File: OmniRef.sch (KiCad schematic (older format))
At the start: 38 parts, among them J1 4mm Banana Jack Pair, J2 4mm Banana Jack Pair, Q1 PMBT3906, SW1 SW_SPDT, U1 REFERENCE IC, U2 LP2951, U3 REFERENCE IC

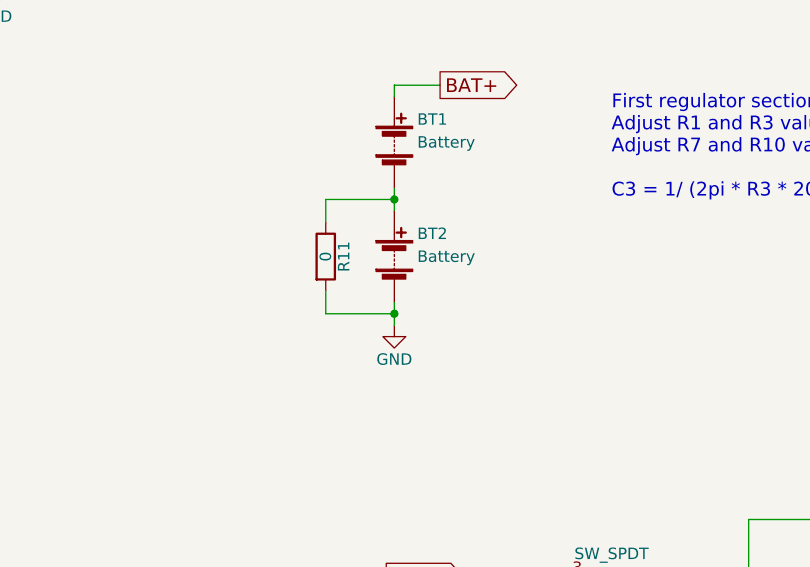
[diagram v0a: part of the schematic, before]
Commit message: Renamed to OmniRef.  Made some final changes to schematic and board before generating gerbers.
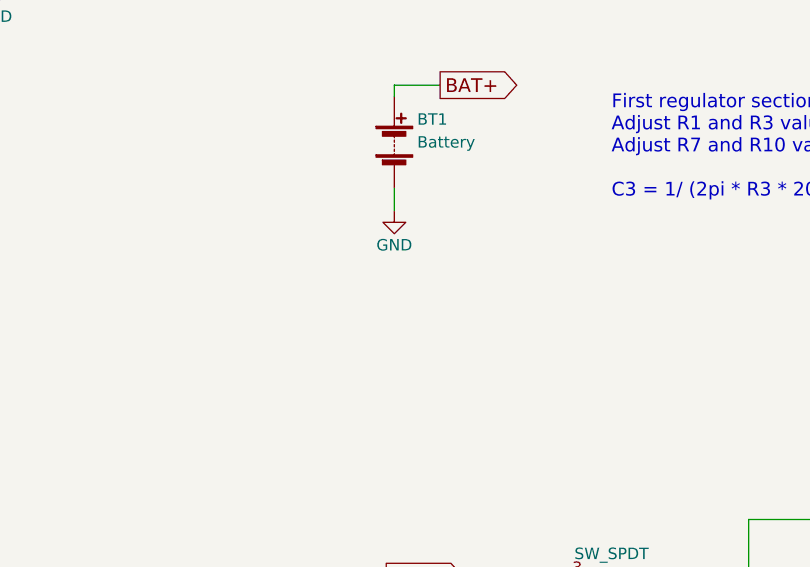
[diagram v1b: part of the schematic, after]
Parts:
- removed BT2: Battery, _NTSFootprints:9vClipWireLeads, symbol Battery
- removed R11: 0, Resistors_SMD:R_0805_HandSoldering, symbol R
- D5, D7: footprint _NTSFootprints:LED_1206_1.7mmHole -> _NTSFootprints:LED_1206_2.15mmHole
- J1: footprint _NTSFootprints:Banana_Jack_2pin_.25_.75 -> _NTSFootprints:Banana_Jack_2pin_Wings_45M_.25_.75
- J2: footprint _NTSFootprints:Banana_Jack_2pin_.25_.75 -> _NTSFootprints:Banana_Jack_2pin_Wings_.25_.75
- SW1: footprint Buttons_Switches_THT:SW_CuK_JS202011CQN_DPDT_Straight -> _NTSFootprints:CnK_L_Series_DPDT
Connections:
- net GND: now also BT1.2 (-)
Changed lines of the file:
@@
 LIBS:elec-unifil
 LIBS:switches
-LIBS:VoltageReference-cache
+LIBS:OmniRef-cache
 EELAYER 25 0
 EELAYER END
@@
 F 0 "D5" H 6550 4350 50  0000 C CNN
 F 1 "LED" H 6550 4150 50  0000 C CNN
-F 2 "_NTSFootprints:LED_1206_1.7mmHole" H 6550 4250 50  0001 C CNN
+F 2 "_NTSFootprints:LED_1206_2.15mmHole" H 6550 4250 50  0001 C CNN
 F 3 "" H 6550 4250 50  0000 C CNN
 	1    6550 4250
@@
 F 0 "J1" H 1150 4300 50  0000 C TNN
 F 1 "4mm Banana Jack Pair" V 1000 4050 50  0000 C TNN
-F 2 "_NTSFootprints:Banana_Jack_2pin_.25_.75" H 1150 3825 50  0001 C CNN
+F 2 "_NTSFootprints:Banana_Jack_2pin_Wings_45M_.25_.75" H 1150 3825 50  0001 C CNN
 F 3 "" H 1125 4050 50  0001 C CNN
 	1    1150 4050
@@
 F 0 "J2" H 5950 6700 50  0000 C TNN
 F 1 "4mm Banana Jack Pair" V 5800 6450 50  0000 C TNN
-F 2 "_NTSFootprints:Banana_Jack_2pin_.25_.75" H 5950 6225 50  0001 C CNN
+F 2 "_NTSFootprints:Banana_Jack_2pin_Wings_.25_.75" H 5950 6225 50  0001 C CNN
 F 3 "" H 5925 6450 50  0001 C CNN
 	1    5950 6450
@@
 F 0 "SW1" H 2000 3620 50  0000 C CNN
 F 1 "SW_SPDT" H 2000 3250 50  0000 C CNN
-F 2 "Buttons_Switches_THT:SW_CuK_JS202011CQN_DPDT_Straight" H 2000 3450 50  0001 C CNN
+F 2 "_NTSFootprints:CnK_L_Series_DPDT" H 2000 3450 50  0001 C CNN
 F 3 "" H 2000 3450 50  0000 C CNN
 	1    2000 3450
@@
 $EndComp
 $Comp
-L Battery BT2
-U 1 1 5A217A5F
-P 1050 1950
-F 0 "BT2" H 1150 2050 50  0000 L CNN
-F 1 "Battery" H 1150 1950 50  0000 L CNN
-F 2 "_NTSFootprints:9vClipWireLeads" V 1050 2010 50  0001 C CNN
-F 3 "" V 1050 2010 50  0000 C CNN
-	1    1050 1950
-	1    0    0    -1
-$EndComp
-$Comp
 L GND #PWR06
 U 1 1 5A218B9C
-P 1050 2250
-F 0 "#PWR06" H 1050 2000 50  0001 C CNN
-F 1 "GND" H 1050 2100 50  0000 C CNN
-F 2 "" H 1050 2250 50  0000 C CNN
-F 3 "" H 1050 2250 50  0000 C CNN
-	1    1050 2250
+P 1050 1750
+F 0 "#PWR06" H 1050 1500 50  0001 C CNN
+F 1 "GND" H 1050 1600 50  0000 C CNN
+F 2 "" H 1050 1750 50  0000 C CNN
+F 3 "" H 1050 1750 50  0000 C CNN
+	1    1050 1750
 	1    0    0    -1
 $EndComp
@@
 F 0 "D7" H 5250 3950 50  0000 C CNN
 F 1 "LED" H 5250 3750 50  0000 C CNN
-F 2 "_NTSFootprints:LED_1206_1.7mmHole" H 5250 3850 50  0001 C CNN
+F 2 "_NTSFootprints:LED_1206_2.15mmHole" H 5250 3850 50  0001 C CNN
 F 3 "" H 5250 3850 50  0000 C CNN
 	1    5250 3850
@@
 Connection ~ 5250 3550
 Connection ~ 5250 4550
-$Comp
-L R R11
-U 1 1 5A2589C2
-P 750 1950
-F 0 "R11" V 830 1950 50  0000 C CNN
-F 1 "0" V 750 1950 50  0000 C CNN
-F 2 "Resistors_SMD:R_0805_HandSoldering" V 680 1950 50  0001 C CNN
-F 3 "" H 750 1950 50  0000 C CNN
-	1    750  1950
-	1    0    0    -1
-$EndComp
-Wire Wire Line
-	750  1800 750  1700
-Wire Wire Line
-	750  1700 1050 1700
-Connection ~ 1050 1700
-Wire Wire Line
-	750  2100 750  2200
-Wire Wire Line
-	750  2200 1050 2200
-Wire Wire Line
-	1050 2150 1050 2250
-Connection ~ 1050 2200
 Wire Wire Line
 	2600 3550 2600 3100

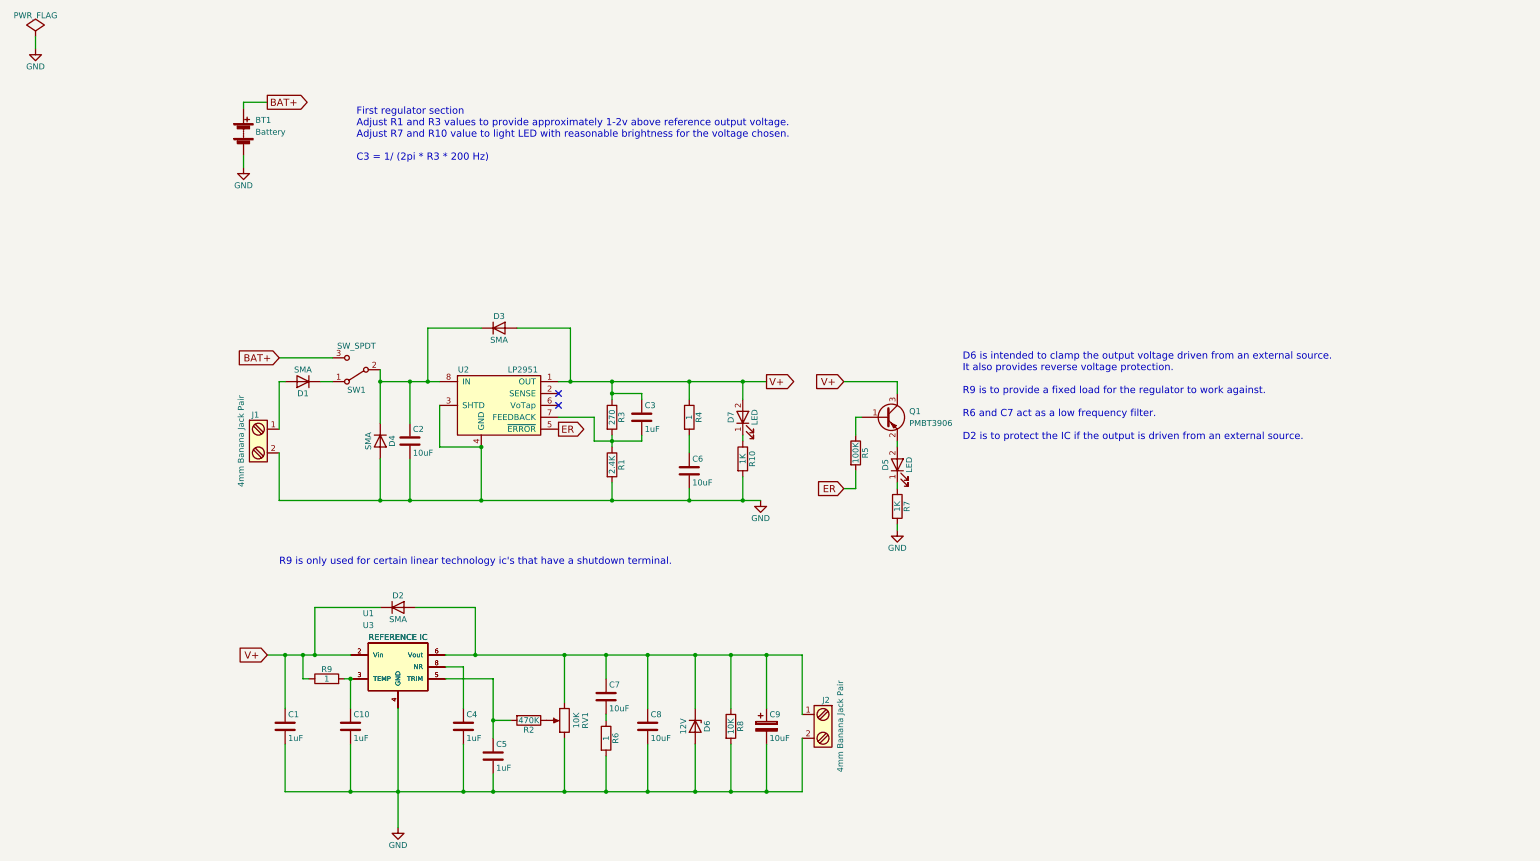
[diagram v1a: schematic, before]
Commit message: Added DC-DC converter front end.  Adjusted some logos and stuff.
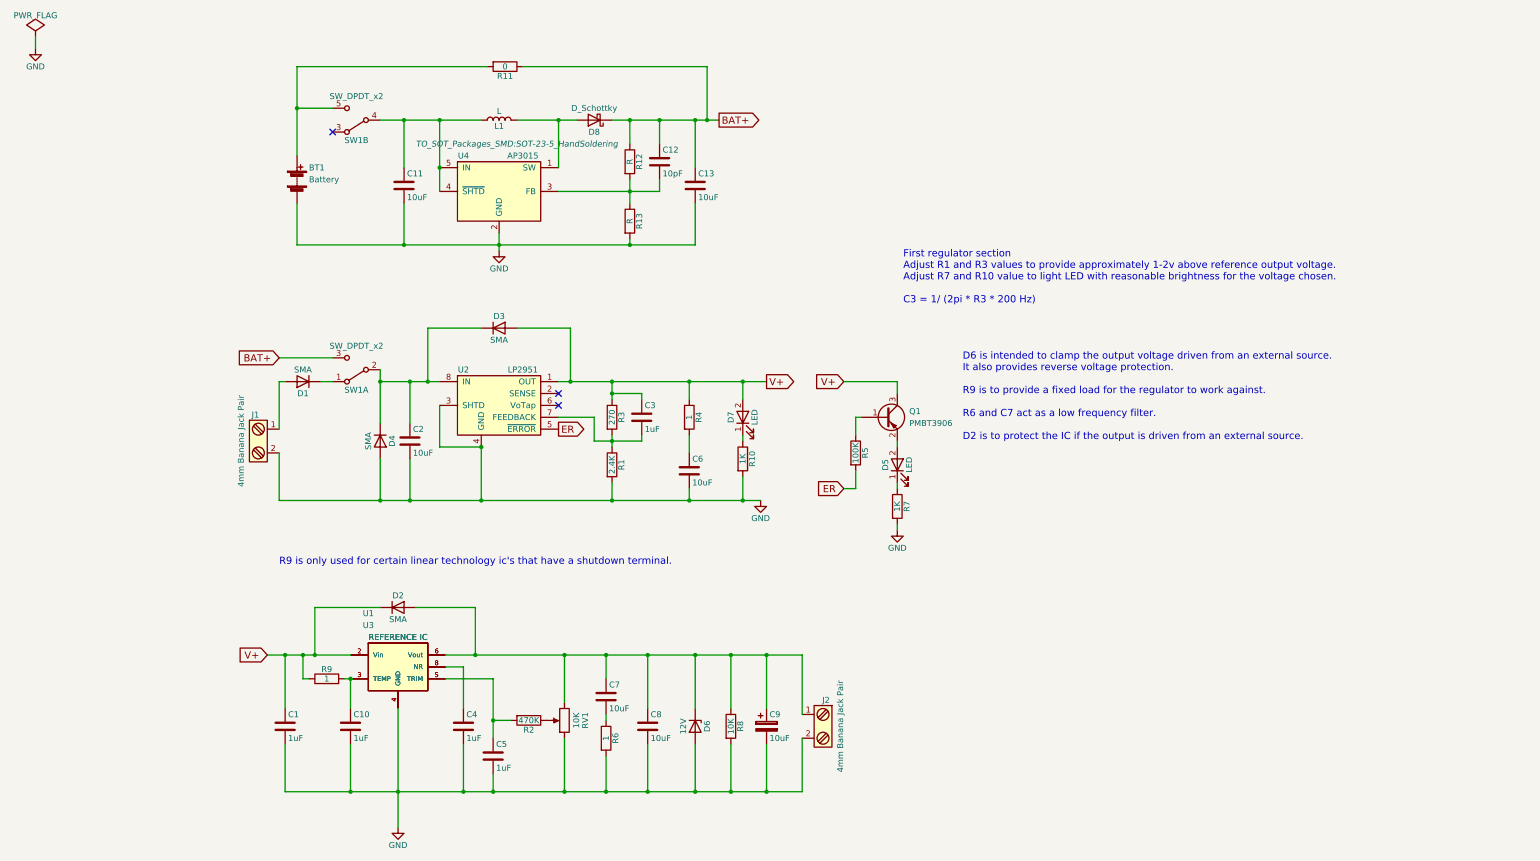
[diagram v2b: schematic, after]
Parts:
- removed SW1: SW_SPDT, _NTSFootprints:CnK_L_Series_DPDT, symbol SW_SPDT
- added C11, C13: 10uF, Capacitors_SMD:C_0805_HandSoldering, symbol C
- added C12: 10pF, Capacitors_SMD:C_0805_HandSoldering, symbol C
- added D8: D_Schottky, Diodes_SMD:D_SMA, symbol D_Schottky
- added L1: L, Inductors:Inductor_Taiyo-Yuden_NR-60xx_HandSoldering, symbol L
- added R11: 0, Resistors_SMD:R_0805_HandSoldering, symbol R
- added R12, R13: R, Resistors_SMD:R_0805_HandSoldering, symbol R
- added SW1: SW_DPDT_x2, _NTSFootprints:CnK_L_Series_DPDT, symbol SW_DPDT_x2
- added U4: AP3015, TO_SOT_Packages_SMD:SOT-23-5_HandSoldering, symbol AP3015
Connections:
- net BAT+: now also C12.1, C13.1, D8.1 (K), R11.1, R12.1, SW1.3 (C); no longer BT1.1 (+)
- net GND: now also C11.2, C13.2, R13.2, U4.2 (GND)
- net at D1.1 (K): now also SW1.1 (A)
- net at C2.1, D3.1 (K), D4.1 (K)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: now also SW1.2 (B)
- new net: BT1.1 (+), R11.2, SW1.5 (C)
- new net: D8.2 (A), L1.2, U4.1 (SW)
- new net: C12.2, R12.2, R13.1, U4.3 (FB)
- new net: C11.1, L1.1, SW1.4 (B), U4.4 (~SHTD), U4.5 (IN)
- no-connect marks 2 -> 3
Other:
- moved on the sheet: BT1
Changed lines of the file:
@@
 LIBS:elec-unifil
 LIBS:switches
+LIBS:ap3015
 LIBS:OmniRef-cache
 EELAYER 25 0
@@
 	1    0    0    -1
 $EndComp
-Text Notes 2000 1700 0    60   ~ 0
+Text Notes 6600 2900 0    60   ~ 0
 First regulator section \nAdjust R1 and R3 values to provide approximately 1-2v above reference output voltage.\nAdjust R7 and R10 value to light LED with reasonable brightness for the voltage chosen.\n\nC3 = 1/ (2pi * R3 * 200 Hz)
 $Comp
@@
 Text GLabel 1350 3350 0    60   Input ~ 0
 BAT+
-$Comp
-L SW_SPDT SW1
-U 1 1 5A216667
-P 2000 3450
-F 0 "SW1" H 2000 3620 50  0000 C CNN
-F 1 "SW_SPDT" H 2000 3250 50  0000 C CNN
-F 2 "_NTSFootprints:CnK_L_Series_DPDT" H 2000 3450 50  0001 C CNN
-F 3 "" H 2000 3450 50  0000 C CNN
-	1    2000 3450
-	-1   0    0    1
-$EndComp
 Wire Wire Line
 	2200 3450 2200 3900
@@
 L Battery BT1
 U 1 1 5A2175D4
-P 1050 1450
-F 0 "BT1" H 1150 1550 50  0000 L CNN
-F 1 "Battery" H 1150 1450 50  0000 L CNN
-F 2 "_NTSFootprints:9vClipWireLeads" V 1050 1510 50  0001 C CNN
-F 3 "" V 1050 1510 50  0000 C CNN
-	1    1050 1450
-	1    0    0    -1
-$EndComp
-$Comp
-L GND #PWR06
-U 1 1 5A218B9C
-P 1050 1750
-F 0 "#PWR06" H 1050 1500 50  0001 C CNN
-F 1 "GND" H 1050 1600 50  0000 C CNN
-F 2 "" H 1050 1750 50  0000 C CNN
-F 3 "" H 1050 1750 50  0000 C CNN
-	1    1050 1750
-	1    0    0    -1
-$EndComp
-Text GLabel 1250 1200 2    60   Output ~ 0
+P 1500 1850
+F 0 "BT1" H 1600 1950 50  0000 L CNN
+F 1 "Battery" H 1600 1850 50  0000 L CNN
+F 2 "_NTSFootprints:9vClipWireLeads" V 1500 1910 50  0001 C CNN
+F 3 "" V 1500 1910 50  0000 C CNN
+	1    1500 1850
+	1    0    0    -1
+$EndComp
+Text GLabel 5050 1350 2    60   Output ~ 0
 BAT+
-Wire Wire Line
-	1050 1200 1250 1200
-Wire Wire Line
-	1050 1200 1050 1250
-Wire Wire Line
-	1050 1650 1050 1750
 $Comp
 L R R10
@@
 Text GLabel 6100 3550 0    60   Input ~ 0
 V+
+$Comp
+L AP3015 U4
+U 1 1 5A37EAC2
+P 3200 1950
+F 0 "U4" H 2900 2250 50  0000 C CNN
+F 1 "AP3015" H 3400 2250 50  0000 C CNN
+F 2 "TO_SOT_Packages_SMD:SOT-23-5_HandSoldering" H 3350 2350 50  0000 C CIN
+F 3 "" H 3200 1950 50  0000 C CNN
+	1    3200 1950
+	1    0    0    -1
+$EndComp
+$Comp
+L SW_DPDT_x2 SW1
+U 1 1 5A37F64C
+P 2000 3450
+F 0 "SW1" H 2000 3620 50  0000 C CNN
+F 1 "SW_DPDT_x2" H 2000 3250 50  0000 C CNN
+F 2 "_NTSFootprints:CnK_L_Series_DPDT" H 2000 3450 50  0001 C CNN
+F 3 "" H 2000 3450 50  0000 C CNN
+	1    2000 3450
+	-1   0    0    1
+$EndComp
+$Comp
+L SW_DPDT_x2 SW1
+U 2 1 5A37F91F
+P 2000 1350
+F 0 "SW1" H 2000 1520 50  0000 C CNN
+F 1 "SW_DPDT_x2" H 2000 1150 50  0000 C CNN
+F 2 "_NTSFootprints:CnK_L_Series_DPDT" H 2000 1350 50  0001 C CNN
+F 3 "" H 2000 1350 50  0000 C CNN
+	2    2000 1350
+	-1   0    0    1
+$EndComp
+$Comp
+L L L1
+U 1 1 5A38050C
+P 3200 1350
+F 0 "L1" V 3150 1350 50  0000 C CNN
+F 1 "L" V 3275 1350 50  0000 C CNN
+F 2 "Inductors:Inductor_Taiyo-Yuden_NR-60xx_HandSoldering" H 3200 1350 50  0001 C CNN
+F 3 "" H 3200 1350 50  0000 C CNN
+	1    3200 1350
+	0    -1   -1   0
+$EndComp
+$Comp
+L D_Schottky D8
+U 1 1 5A380610
+P 4000 1350
+F 0 "D8" H 4000 1450 50  0000 C CNN
+F 1 "D_Schottky" H 4000 1250 50  0000 C CNN
+F 2 "Diodes_SMD:D_SMA" H 4000 1350 50  0001 C CNN
+F 3 "" H 4000 1350 50  0000 C CNN
+	1    4000 1350
+	-1   0    0    1
+$EndComp
+Wire Wire Line
+	4150 1350 5050 1350
+Wire Wire Line
+	3700 1750 3700 1350
+Connection ~ 3700 1350
+Wire Wire Line
+	2200 1350 3050 1350
+Wire Wire Line
+	2700 1350 2700 1950
+Connection ~ 2700 1350
+Connection ~ 2700 1750
+Wire Wire Line
+	3350 1350 3850 1350
+Wire Wire Line
+	3700 1950 4550 1950
+Connection ~ 4300 1350
+NoConn ~ 1800 1450
+$Comp
+L GND #PWR06
+U 1 1 5A382251
+P 3200 2450
+F 0 "#PWR06" H 3200 2200 50  0001 C CNN
+F 1 "GND" H 3200 2300 50  0000 C CNN
+F 2 "" H 3200 2450 50  0000 C CNN
+F 3 "" H 3200 2450 50  0000 C CNN
+	1    3200 2450
+	1    0    0    -1
+$EndComp
+Wire Wire Line
+	3200 2300 3200 2450
+$Comp
+L R R12
+U 1 1 5A3824A1
+P 4300 1700
+F 0 "R12" V 4380 1700 50  0000 C CNN
+F 1 "R" V 4300 1700 50  0000 C CNN
+F 2 "Resistors_SMD:R_0805_HandSoldering" V 4230 1700 50  0001 C CNN
+F 3 "" H 4300 1700 50  0000 C CNN
+	1    4300 1700
+	1    0    0    -1
+$EndComp
+$Comp
+L R R13
+U 1 1 5A3825B0
+P 4300 2200
+F 0 "R13" V 4380 2200 50  0000 C CNN
+F 1 "R" V 4300 2200 50  0000 C CNN
+F 2 "Resistors_SMD:R_0805_HandSoldering" V 4230 2200 50  0001 C CNN
+F 3 "" H 4300 2200 50  0000 C CNN
+	1    4300 2200
+	1    0    0    -1
+$EndComp
+$Comp
+L C C12
+U 1 1 5A382632
+P 4550 1700
+F 0 "C12" H 4575 1800 50  0000 L CNN
+F 1 "10pF" H 4575 1600 50  0000 L CNN
+F 2 "Capacitors_SMD:C_0805_HandSoldering" H 4588 1550 50  0001 C CNN
+F 3 "" H 4550 1700 50  0000 C CNN
+	1    4550 1700
+	1    0    0    -1
+$EndComp
+$Comp
+L C C11
+U 1 1 5A382944
+P 2400 1900
+F 0 "C11" H 2425 2000 50  0000 L CNN
+F 1 "10uF" H 2425 1800 50  0000 L CNN
+F 2 "Capacitors_SMD:C_0805_HandSoldering" H 2438 1750 50  0001 C CNN
+F 3 "" H 2400 1900 50  0000 C CNN
+	1    2400 1900
+	1    0    0    -1
+$EndComp
+Wire Wire Line
+	1500 2400 4850 2400
+Connection ~ 3200 2400
+Connection ~ 2400 1350
+Wire Wire Line
+	4300 2400 4300 2350
+Wire Wire Line
+	4300 1850 4300 2050
+Connection ~ 4300 1950
+Wire Wire Line
+	4550 1950 4550 1850
+Wire Wire Line
+	4550 1550 4550 1350
+Connection ~ 4550 1350
+Wire Wire Line
+	4300 1550 4300 1350
+$Comp
+L C C13
+U 1 1 5A3834FD
+P 4850 1900
+F 0 "C13" H 4875 2000 50  0000 L CNN
+F 1 "10uF" H 4875 1800 50  0000 L CNN
+F 2 "Capacitors_SMD:C_0805_HandSoldering" H 4888 1750 50  0001 C CNN
+F 3 "" H 4850 1900 50  0000 C CNN
+	1    4850 1900
+	1    0    0    -1
+$EndComp
+Connection ~ 4300 2400
+Connection ~ 4850 1350
+Connection ~ 2400 2400
+Wire Wire Line
+	1500 1250 1800 1250
+Wire Wire Line
+	1500 900  1500 1650
+Wire Wire Line
+	1500 2050 1500 2400
+Wire Wire Line
+	2400 1750 2400 1350
+Wire Wire Line
+	2400 2050 2400 2400
+Wire Wire Line
+	4850 2400 4850 2050
+Wire Wire Line
+	4850 1750 4850 1350
+$Comp
+L R R11
+U 1 1 5A3861CA
+P 3250 900
+F 0 "R11" V 3330 900 50  0000 C CNN
+F 1 "0" V 3250 900 50  0000 C CNN
+F 2 "Resistors_SMD:R_0805_HandSoldering" V 3180 900 50  0001 C CNN
+F 3 "" H 3250 900 50  0000 C CNN
+	1    3250 900
+	0    1    1    0
+$EndComp
+Wire Wire Line
+	1500 900  3100 900
+Connection ~ 1500 1250
+Wire Wire Line
+	3400 900  4950 900
+Wire Wire Line
+	4950 900  4950 1350
+Connection ~ 4950 1350
 $EndSCHEMATC
